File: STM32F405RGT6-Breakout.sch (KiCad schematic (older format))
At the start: 23 parts

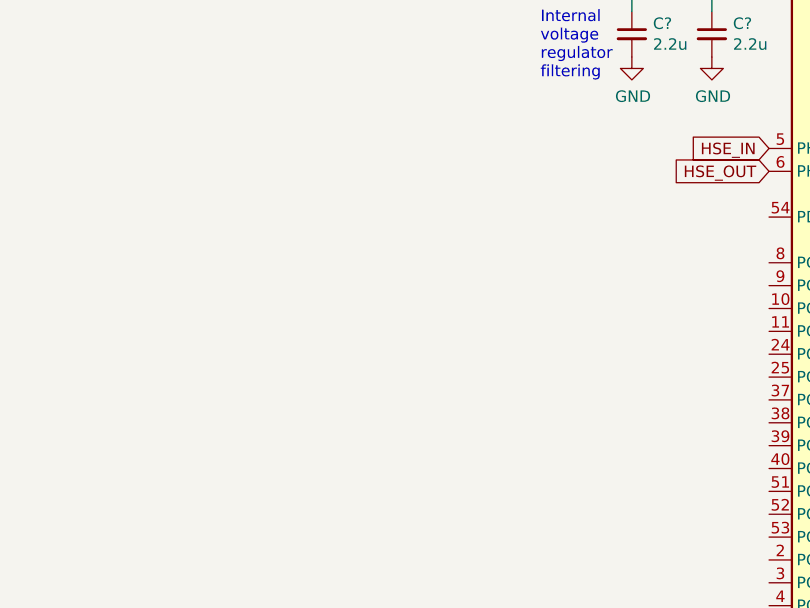
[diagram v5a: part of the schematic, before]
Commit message: Crystal oscillator
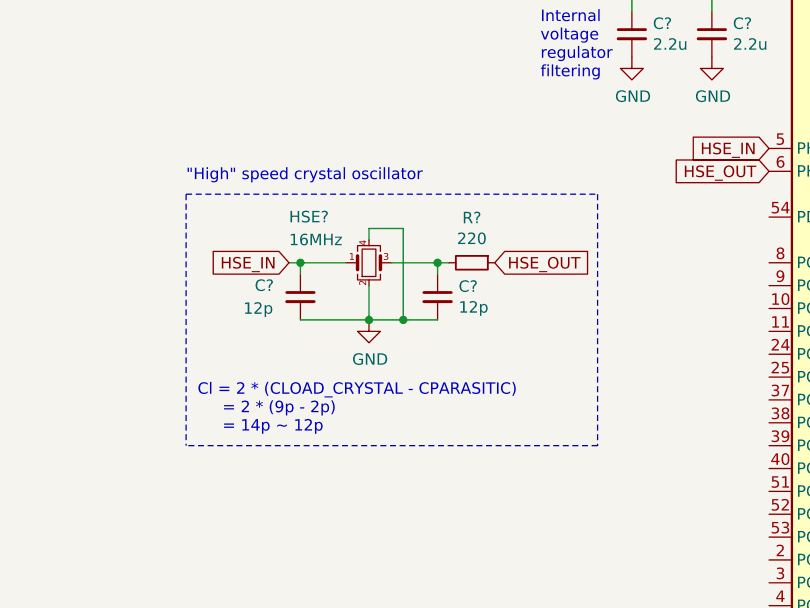
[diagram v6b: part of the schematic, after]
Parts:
- added C? (x2): 12p, symbol Device:C_Small
- added HSE?: 16MHz, symbol Device:Crystal_GND24_Small
- added R?: 220, symbol Device:R_Small
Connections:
- net GND: now also C?.2, C?.2, HSE?.2, HSE?.4
- net HSE_IN: now also C?.1, HSE?.1
- net HSE_OUT: now also R?.1
- new net: C?.1, HSE?.3, R?.2
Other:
- note added: ""High" speed crystal oscillator"
- note added: "Cl = 2 * (CLOAD_CRYSTAL - CPARASITIC)\n = 2 * (9p - 2p)\n = 14p ~~ 12p"
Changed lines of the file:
@@
 Text GLabel 5550 4000 0    50   Input ~ 0
 HSE_OUT
+$Comp
+L Device:Crystal_GND24_Small HSE?
+U 1 1 619D5B8C
+P 3800 4400
+F 0 "HSE?" H 3450 4600 50  0000 L CNN
+F 1 "16MHz" H 3450 4500 50  0000 L CNN
+F 2 "" H 3800 4400 50  0001 C CNN
+F 3 "~" H 3800 4400 50  0001 C CNN
+	1    3800 4400
+	1    0    0    -1
+$EndComp
+$Comp
+L power:GND #PWR?
+U 1 1 619D8425
+P 3800 4650
+F 0 "#PWR?" H 3800 4400 50  0001 C CNN
+F 1 "GND" H 3805 4477 50  0000 C CNN
+F 2 "" H 3800 4650 50  0001 C CNN
+F 3 "" H 3800 4650 50  0001 C CNN
+	1    3800 4650
+	1    0    0    -1
+$EndComp
+Text GLabel 4350 4400 2    50   Input ~ 0
+HSE_OUT
+$Comp
+L Device:R_Small R?
+U 1 1 619D92E6
+P 4250 4400
+F 0 "R?" V 4054 4400 50  0000 C CNN
+F 1 "220" V 4145 4400 50  0000 C CNN
+F 2 "" H 4250 4400 50  0001 C CNN
+F 3 "~" H 4250 4400 50  0001 C CNN
+	1    4250 4400
+	0    1    1    0
+$EndComp
+Wire Wire Line
+	4150 4400 4100 4400
+$Comp
+L Device:C_Small C?
+U 1 1 619DB81B
+P 4100 4550
+F 0 "C?" H 4192 4596 50  0000 L CNN
+F 1 "12p" H 4192 4505 50  0000 L CNN
+F 2 "" H 4100 4550 50  0001 C CNN
+F 3 "~" H 4100 4550 50  0001 C CNN
+	1    4100 4550
+	1    0    0    -1
+$EndComp
+Wire Wire Line
+	4100 4450 4100 4400
+Connection ~ 4100 4400
+Wire Wire Line
+	3800 4300 3800 4250
+Wire Wire Line
+	3800 4250 3950 4250
+Wire Wire Line
+	3950 4250 3950 4650
+Wire Wire Line
+	3950 4650 3800 4650
+Wire Wire Line
+	3900 4400 4100 4400
+Wire Wire Line
+	3950 4650 4100 4650
+Connection ~ 3950 4650
+Connection ~ 3800 4650
+Wire Wire Line
+	3500 4400 3700 4400
+Connection ~ 3500 4400
+Wire Wire Line
+	3500 4450 3500 4400
+Wire Wire Line
+	3500 4650 3800 4650
+Wire Wire Line
+	3450 4400 3500 4400
+$Comp
+L Device:C_Small C?
+U 1 1 619DBEC1
+P 3500 4550
+F 0 "C?" H 3300 4600 50  0000 L CNN
+F 1 "12p" H 3250 4500 50  0000 L CNN
+F 2 "" H 3500 4550 50  0001 C CNN
+F 3 "~" H 3500 4550 50  0001 C CNN
+	1    3500 4550
+	1    0    0    -1
+$EndComp
+Text GLabel 3450 4400 0    50   Input ~ 0
+HSE_IN
+Wire Wire Line
+	3800 4500 3800 4650
+Text Notes 3050 5150 0    50   ~ 0
+Cl = 2 * (CLOAD_CRYSTAL - CPARASITIC)\n     = 2 * (9p - 2p)\n     = 14p ~~ 12p
+Wire Notes Line
+	4800 5200 3000 5200
+Wire Notes Line
+	3000 4100 4800 4100
+Wire Notes Line
+	3000 4100 3000 5200
+Wire Notes Line
+	4800 4100 4800 5200
+Text Notes 3000 4050 0    50   ~ 0
+"High" speed crystal oscillator
 $EndSCHEMATC

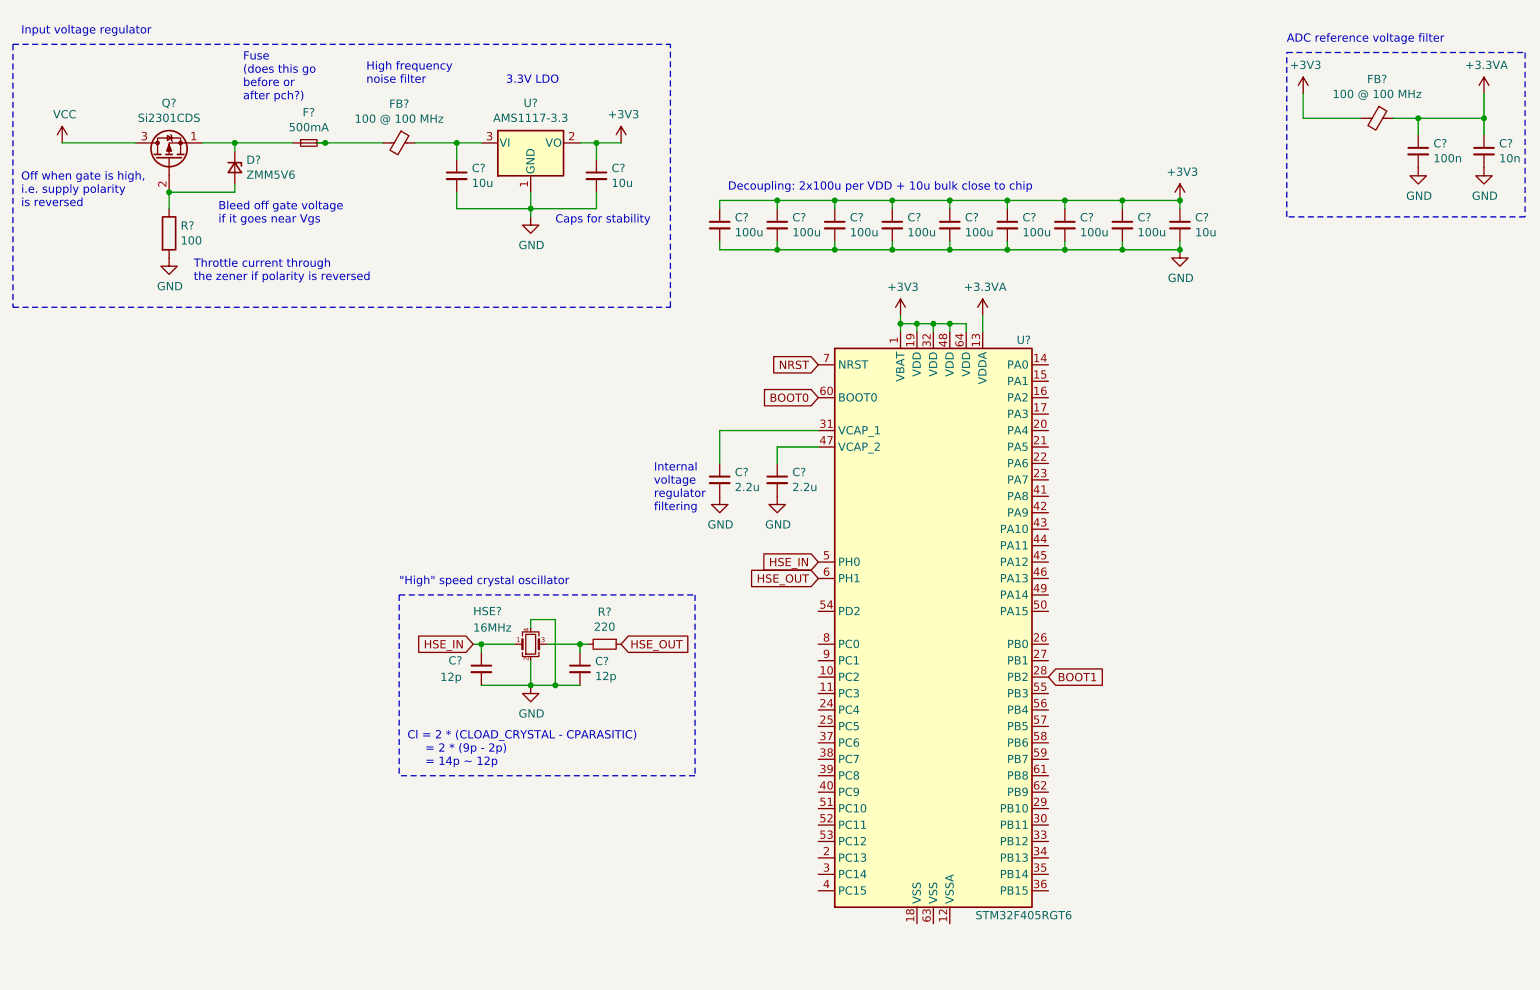
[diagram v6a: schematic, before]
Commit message: Hook up serial wire debug & enable on chip
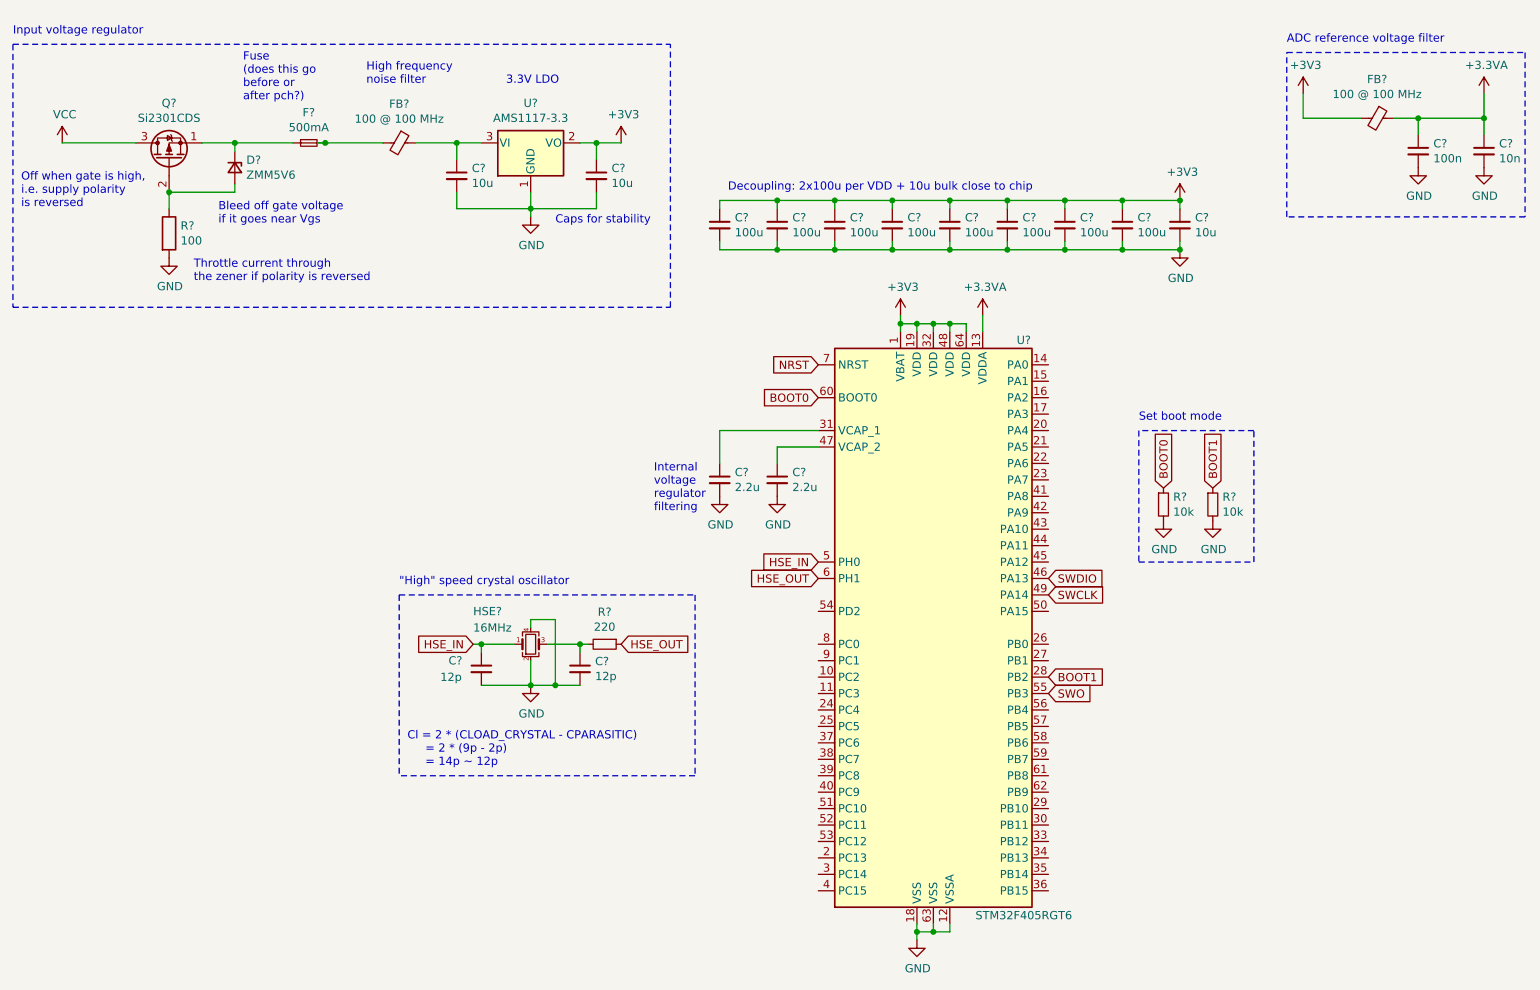
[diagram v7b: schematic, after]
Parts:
- added R? (x2): 10k, symbol Device:R_Small
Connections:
- net BOOT0: now also R?.1
- net BOOT1: now also R?.1
- net GND: now also U?.12 (VSSA), U?.18 (VSS), U?.63 (VSS), R?.2, R?.2
- net SWDIO: now reaches U?.46 (PA13)
- net SWCLK: now reaches U?.49 (PA14)
- net SWO: now reaches U?.55 (PB3)
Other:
- note added: "Set boot mode"
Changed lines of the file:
@@
 Wire Notes Line
 	650  750  4650 750
-Text Notes 700  700  0    50   ~ 0
-Input voltage regulator
 $Comp
 L power:+3V3 #PWR?
@@
 Wire Notes Line
 	8400 800  9850 800
-Text Notes 8400 750  0    50   ~ 0
-ADC reference voltage filter\n
 $Comp
 L Device:C_Small C?
@@
 Wire Wire Line
 	4950 1950 4950 2000
-Text Notes 5000 1650 0    50   ~ 0
-Decoupling: 2x100u per VDD + 10u bulk close to chip
 Connection ~ 7750 1700
 Connection ~ 7750 2000
@@
 F 3 "" H 4950 3500 50  0001 C CNN
 	1    4950 3500
-	1    0    0    -1
-$EndComp
-$Comp
-L power:GND #PWR?
-U 1 1 619D0B27
-P 5300 3500
-F 0 "#PWR?" H 5300 3250 50  0001 C CNN
-F 1 "GND" H 5305 3327 50  0000 C CNN
-F 2 "" H 5300 3500 50  0001 C CNN
-F 3 "" H 5300 3500 50  0001 C CNN
-	1    5300 3500
 	1    0    0    -1
 $EndComp
@@
 Wire Notes Line
 	4800 4100 4800 5200
+$Comp
+L Device:R_Small R?
+U 1 1 61A1AA95
+P 7650 3550
+F 0 "R?" H 7709 3596 50  0000 L CNN
+F 1 "10k" H 7709 3505 50  0000 L CNN
+F 2 "" H 7650 3550 50  0001 C CNN
+F 3 "~" H 7650 3550 50  0001 C CNN
+	1    7650 3550
+	1    0    0    -1
+$EndComp
+$Comp
+L Device:R_Small R?
+U 1 1 61A1B70C
+P 7950 3550
+F 0 "R?" H 8009 3596 50  0000 L CNN
+F 1 "10k" H 8009 3505 50  0000 L CNN
+F 2 "" H 7950 3550 50  0001 C CNN
+F 3 "~" H 7950 3550 50  0001 C CNN
+	1    7950 3550
+	1    0    0    -1
+$EndComp
+Text GLabel 7950 3450 1    50   Input ~ 0
+BOOT1
+Text GLabel 7650 3450 1    50   Input ~ 0
+BOOT0
+$Comp
+L power:GND #PWR?
+U 1 1 61A1C688
+P 7650 3650
+F 0 "#PWR?" H 7650 3400 50  0001 C CNN
+F 1 "GND" H 7655 3477 50  0000 C CNN
+F 2 "" H 7650 3650 50  0001 C CNN
+F 3 "" H 7650 3650 50  0001 C CNN
+	1    7650 3650
+	1    0    0    -1
+$EndComp
+$Comp
+L power:GND #PWR?
+U 1 1 61A1CBA1
+P 7950 3650
+F 0 "#PWR?" H 7950 3400 50  0001 C CNN
+F 1 "GND" H 7955 3477 50  0000 C CNN
+F 2 "" H 7950 3650 50  0001 C CNN
+F 3 "" H 7950 3650 50  0001 C CNN
+	1    7950 3650
+	1    0    0    -1
+$EndComp
+Wire Notes Line
+	7500 3100 7500 3900
+Wire Notes Line
+	7500 3900 8200 3900
+Wire Notes Line
+	8200 3900 8200 3100
+Wire Notes Line
+	8200 3100 7500 3100
+Text Notes 7500 3050 0    50   ~ 0
+Set boot mode
+Text Notes 8400 750  0    50   ~ 0
+ADC reference voltage filter\n
+Text Notes 650  700  0    50   ~ 0
+Input voltage regulator
 Text Notes 3000 4050 0    50   ~ 0
 "High" speed crystal oscillator
+Text GLabel 6950 4000 2    50   Input ~ 0
+SWDIO
+Text GLabel 6950 4100 2    50   Input ~ 0
+SWCLK
+Text GLabel 6950 4700 2    50   Input ~ 0
+SWO
+$Comp
+L power:GND #PWR?
+U 1 1 619D0B27
+P 5300 3500
+F 0 "#PWR?" H 5300 3250 50  0001 C CNN
+F 1 "GND" H 5305 3327 50  0000 C CNN
+F 2 "" H 5300 3500 50  0001 C CNN
+F 3 "" H 5300 3500 50  0001 C CNN
+	1    5300 3500
+	1    0    0    -1
+$EndComp
+$Comp
+L power:GND #PWR?
+U 1 1 61A2A7A4
+P 6150 6200
+F 0 "#PWR?" H 6150 5950 50  0001 C CNN
+F 1 "GND" H 6155 6027 50  0000 C CNN
+F 2 "" H 6150 6200 50  0001 C CNN
+F 3 "" H 6150 6200 50  0001 C CNN
+	1    6150 6200
+	1    0    0    -1
+$EndComp
+Wire Wire Line
+	6150 6100 6150 6150
+Wire Wire Line
+	6350 6100 6350 6150
+Wire Wire Line
+	6350 6150 6250 6150
+Connection ~ 6150 6150
+Wire Wire Line
+	6250 6100 6250 6150
+Connection ~ 6250 6150
+Wire Wire Line
+	6250 6150 6150 6150
+Wire Wire Line
+	6150 6150 6150 6200
+Text Notes 5000 1650 0    50   ~ 0
+Decoupling: 2x100u per VDD + 10u bulk close to chip
 $EndSCHEMATC

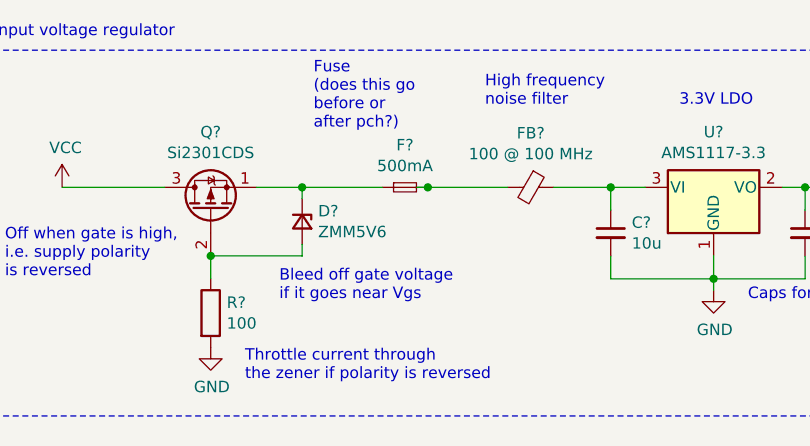
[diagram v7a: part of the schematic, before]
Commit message: fixed an unconnected pin
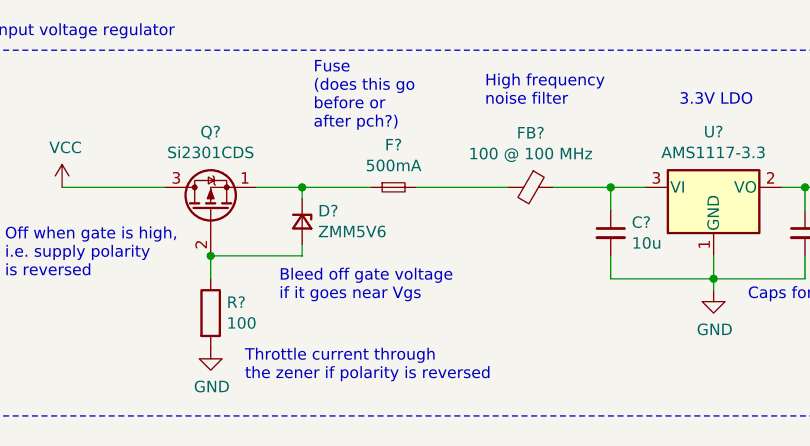
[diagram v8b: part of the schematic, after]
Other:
- moved on the sheet: F?
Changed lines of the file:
@@
 L Device:Fuse_Small F?
 U 1 1 61935A18
-P 2450 1350
-F 0 "F?" H 2450 1535 50  0000 C CNN
-F 1 "500mA" H 2450 1444 50  0000 C CNN
-F 2 "" H 2450 1350 50  0001 C CNN
-F 3 "~" H 2450 1350 50  0001 C CNN
-	1    2450 1350
+P 2400 1350
+F 0 "F?" H 2400 1535 50  0000 C CNN
+F 1 "500mA" H 2400 1444 50  0000 C CNN
+F 2 "" H 2400 1350 50  0001 C CNN
+F 3 "~" H 2400 1350 50  0001 C CNN
+	1    2400 1350
 	1    0    0    -1
 $EndComp
@@
 	2000 1400 2000 1350
 Wire Wire Line
-	2500 1350 2550 1350
-Wire Wire Line
 	3100 1350 3350 1350
 $Comp
@@
 	2000 1350 1800 1350
 Wire Wire Line
-	2000 1350 2350 1350
+	2000 1350 2300 1350
 Text Notes 1900 1850 0    50   ~ 0
 Bleed off gate voltage \nif it goes near Vgs
@@
 Wire Wire Line
 	4200 1350 4100 1350
-Connection ~ 2550 1350
 Wire Wire Line
-	2550 1350 2900 1350
+	2500 1350 2900 1350
 Text Notes 3950 1850 0    50   ~ 0
 Caps for stability\n
